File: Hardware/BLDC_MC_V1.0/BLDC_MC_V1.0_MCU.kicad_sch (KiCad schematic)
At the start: 47 parts, among them J3 USB_C_Receptacle_USB2.0_16P, J4 Conn_02x03_Counter_Clockwise, SW1 SW_Push, U4 STM32G431RBT6, U9 USBLC6-2SC6, Y1 7M-24.000MAAJ-T, Y2 ABS07-32.768KHZ-T

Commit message: Update board layout
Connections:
- net U_P: now reaches J3.A7 (D-), J3.B7 (D-), U9.1 (I/O1)
- net U_N: now reaches J3.A6 (D+), J3.B6 (D+), U9.3 (I/O2)
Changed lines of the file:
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@@
+		)
+	)
+	(label "U_N"
+		(at 240.03 137.16 0)
+		(effects
+			(font
+				(size 1.27 1.27)
+			)
+			(justify left bottom)
+		)
+	)
+	(label "U_P"
+		(at 240.03 134.62 0)
+		(effects
+			(font
+				(size 1.27 1.27)
+			)
+			(justify left bottom)
 		)
 	)

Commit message: Update the layout of the board by routing the connections between controller and gate drive
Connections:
- net SOA: now also U4.14 (PA2); no longer U4.12 (PA0)
- net SOC: now also U4.12 (PA0); no longer U4.14 (PA2)
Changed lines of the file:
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@@
 	(wire
 		(pts
+			(xy 120.65 66.04) (xy 125.73 66.04)
+		)
+		(stroke
+			(width 0)
+			(type default)
+		)
+	)
+	(wire
+		(pts
 			(xy 107.95 50.8) (xy 107.95 58.42)
 		)
@@
 	(wire
 		(pts
-			(xy 120.65 71.12) (xy 125.73 71.12)
+			(xy 66.04 121.92) (xy 66.04 123.19)
 		)
 		(stroke
@@
 	(wire
 		(pts
-			(xy 66.04 121.92) (xy 66.04 123.19)
+			(xy 233.68 78.74) (xy 242.57 78.74)
 		)
 		(stroke
@@
 	(wire
 		(pts
-			(xy 233.68 78.74) (xy 242.57 78.74)
+			(xy 82.55 139.7) (xy 85.09 139.7)
 		)
 		(stroke
@@
 	(wire
 		(pts
-			(xy 82.55 139.7) (xy 85.09 139.7)
+			(xy 240.03 139.7) (xy 243.84 139.7)
 		)
 		(stroke
@@
 	(wire
 		(pts
-			(xy 240.03 139.7) (xy 243.84 139.7)
+			(xy 132.08 86.36) (xy 148.59 86.36)
 		)
 		(stroke
@@
 	(wire
 		(pts
-			(xy 132.08 86.36) (xy 148.59 86.36)
+			(xy 57.15 134.62) (xy 59.69 134.62)
 		)
 		(stroke
@@
 	(wire
 		(pts
-			(xy 57.15 134.62) (xy 59.69 134.62)
+			(xy 269.24 76.2) (xy 275.59 76.2)
 		)
 		(stroke
@@
 	(wire
 		(pts
-			(xy 269.24 76.2) (xy 275.59 76.2)
+			(xy 120.65 71.12) (xy 125.73 71.12)
 		)
 		(stroke
@@
 	(wire
 		(pts
-			(xy 120.65 68.58) (xy 125.73 68.58)
-		)
-		(stroke
-			(width 0)
-			(type default)
-		)
-	)
-	(wire
-		(pts
 			(xy 132.08 111.76) (xy 148.59 111.76)
 		)
@@
 	(wire
 		(pts
+			(xy 120.65 68.58) (xy 125.73 68.58)
+		)
+		(stroke
+			(width 0)
+			(type default)
+		)
+	)
+	(wire
+		(pts
 			(xy 243.84 124.46) (xy 243.84 127)
 		)
@@
 	(wire
 		(pts
-			(xy 120.65 66.04) (xy 125.73 66.04)
-		)
-		(stroke
-			(width 0)
-			(type default)
-		)
-	)
-	(wire
-		(pts
 			(xy 262.89 34.29) (xy 251.46 34.29)
 		)
@@
 	(hierarchical_label "SOC"
 		(shape input)
-		(at 125.73 71.12 0)
+		(at 125.73 66.04 0)
 		(effects
 			(font
@@
 	(hierarchical_label "SOA"
 		(shape input)
-		(at 125.73 66.04 0)
+		(at 125.73 71.12 0)
 		(effects
 			(font
@@
 		)
 	)
-	(embedded_fonts no)
 )

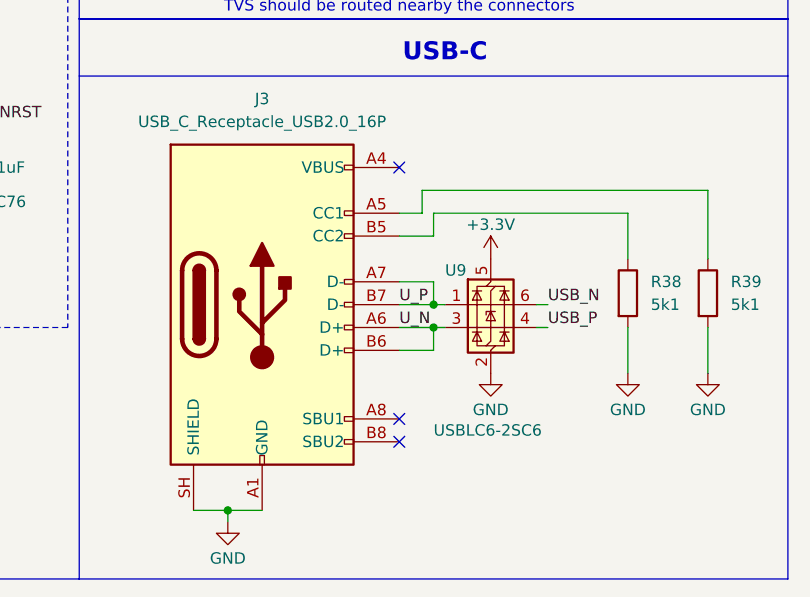
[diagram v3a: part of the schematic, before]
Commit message: Solve most of ERC errors
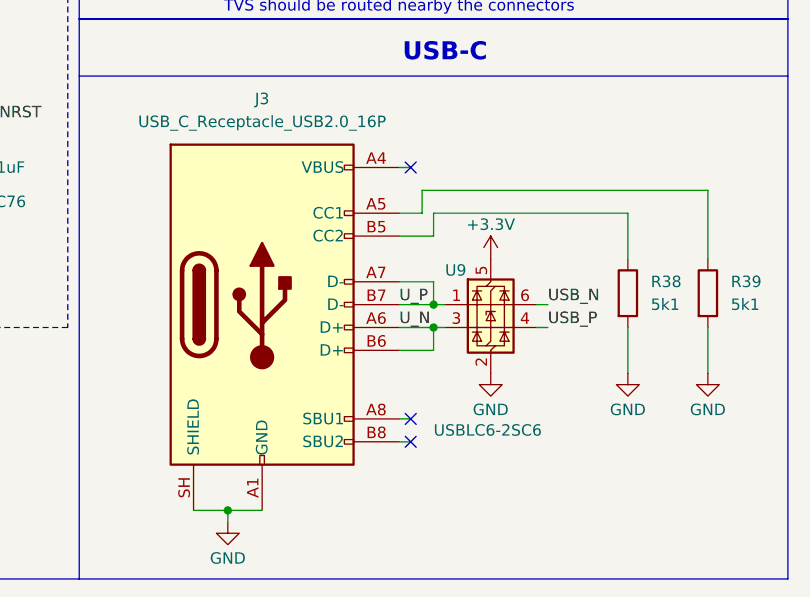
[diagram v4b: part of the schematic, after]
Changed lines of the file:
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@@
 	)
 	(no_connect
-		(at 240.03 147.32)
+		(at 241.3 147.32)
 	)
 	(no_connect
@@
 	)
 	(no_connect
-		(at 240.03 149.86)
+		(at 241.3 149.86)
 	)
 	(no_connect
@@
 	)
 	(no_connect
-		(at 240.03 119.38)
+		(at 241.3 119.38)
 	)
 	(no_connect
@@
 	(wire
 		(pts
+			(xy 241.3 119.38) (xy 240.03 119.38)
+		)
+		(stroke
+			(width 0)
+			(type default)
+		)
+	)
+	(wire
+		(pts
 			(xy 275.59 34.29) (xy 262.89 34.29)
 		)
@@
 	(wire
 		(pts
+			(xy 241.3 149.86) (xy 240.03 149.86)
+		)
+		(stroke
+			(width 0)
+			(type default)
+		)
+	)
+	(wire
+		(pts
 			(xy 82.55 111.76) (xy 85.09 111.76)
 		)
@@
 		)
 		(stroke
+			(width 0)
+			(type default)
+		)
+	)
+	(wire
+		(pts
+			(xy 241.3 147.32) (xy 240.03 147.32)
+		)
+		(stroke

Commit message: Solved all the worrnings founded
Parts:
- J3: footprint Connector_USB:USB_C_Receptacle_GCT_USB4105-xx-A_16P_TopMnt_Horizontal -> BLDC_Motor_Driver_Components_Footprint:USB_C_Receptacle_GCT_USB4105-xx-A_16P_TopMnt_Horizontal
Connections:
- net GND: no longer J3.B1 (GND), J3.B12 (GND)
- net at J3.A4 (VBUS), J3.A9 (VBUS): no longer J3.B4 (VBUS), J3.B9 (VBUS)
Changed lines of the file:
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@@
 			)
 		)
-		(property "Footprint" "Connector_USB:USB_C_Receptacle_GCT_USB4105-xx-A_16P_TopMnt_Horizontal"
+		(property "Footprint" "BLDC_Motor_Driver_Components_Footprint:USB_C_Receptacle_GCT_USB4105-xx-A_16P_TopMnt_Horizontal"
 			(at 228.6 134.62 0)
 			(hide yes)
@@
 			)
 		)
-		(pin "B4"
-		)
-		(pin "B12"
-		)
 		(pin "SH"
 		)
@@
 		)
 		(pin "A12"
-		)
-		(pin "B1"
 		)
 		(pin "A4"
@@
 		(pin "B5"
 		)
-		(pin "B9"
-		)
 		(pin "A7"

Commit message: Edited the label of the Schematic sheets
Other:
- company: (none) -> Ahmed Aboeita
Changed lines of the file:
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@@
 	(title_block
 		(title "${Project_Name}")
-		(date "2026-03-23")
-		(rev "V1")
+		(date "2026-08-17")
+		(rev "V1.0")
+		(company "Ahmed Aboeita")
+		(comment 1 "8-Layer High-TG180 PCB with Kelvin Current Sensing")
+		(comment 2 "Power Stage: 3-Phase Inverter with Active Reverse Polarity & E-Fuse OCP")
+		(comment 3 "Core MCU: STM32G431RBT6 (FOC & CORDIC Processing, 100 kHz PWM)")
+		(comment 4 "Stackup & Sensing: System Ratings: 100V DC Bus | 50A Continuous | T_A = 125 degrees  ")
 	)
 	(rectangle
